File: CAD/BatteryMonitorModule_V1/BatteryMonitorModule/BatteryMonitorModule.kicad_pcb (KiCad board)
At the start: 2 copper layers, 76.2 x 101.6 mm, 85 parts, among them J1 OSTYK42105030, J10 J_DISP_SPI, J11 J_UART, J12 J_EXP_B, J13 J_EXP_A, J2 OSTYK42102030, J3 Conn_ARM_JTAG_SWD_10, J4 USB-C, J5 J_FAN, J6 J_FAN_SEL, J7 J_NFC, J8 J_PANEL, K1 G5LE-1, Q1 AO3401A, Q2 IRFZ44NPBF, Q3 MMBT2222A, Q4 MMBT2222A, Q5 2N7002, SW1 BOOT0, SW2 NRST, U1 STM32G0B1CCT6, U2 INA226AQDGSRQ1, U3 AP63205WU-7, U4 TC2117-3.3VDBTR

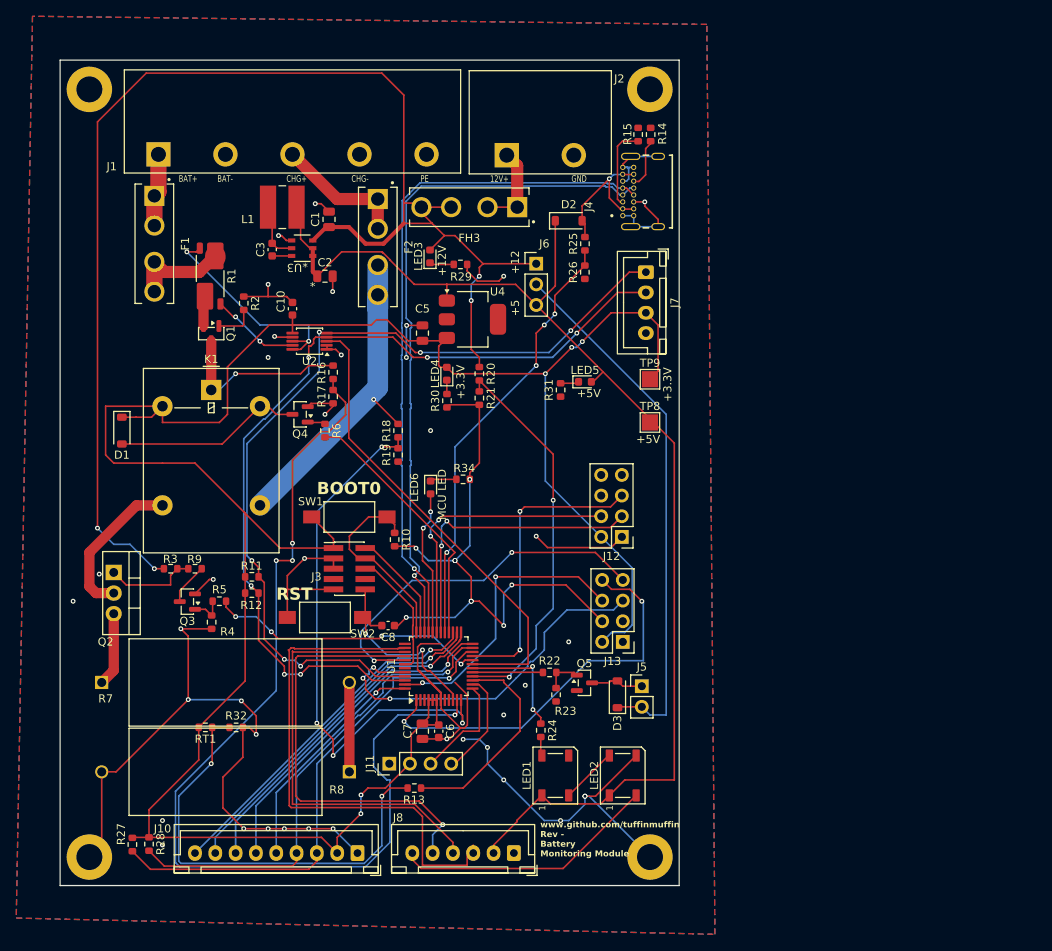
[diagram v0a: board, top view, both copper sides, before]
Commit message: V1 PCB layout updates and QT06ADP83H0000G footprint refinement
Co-Authored-By: Claude Opus 4.7 (1M context) <noreply@anthropic.com>
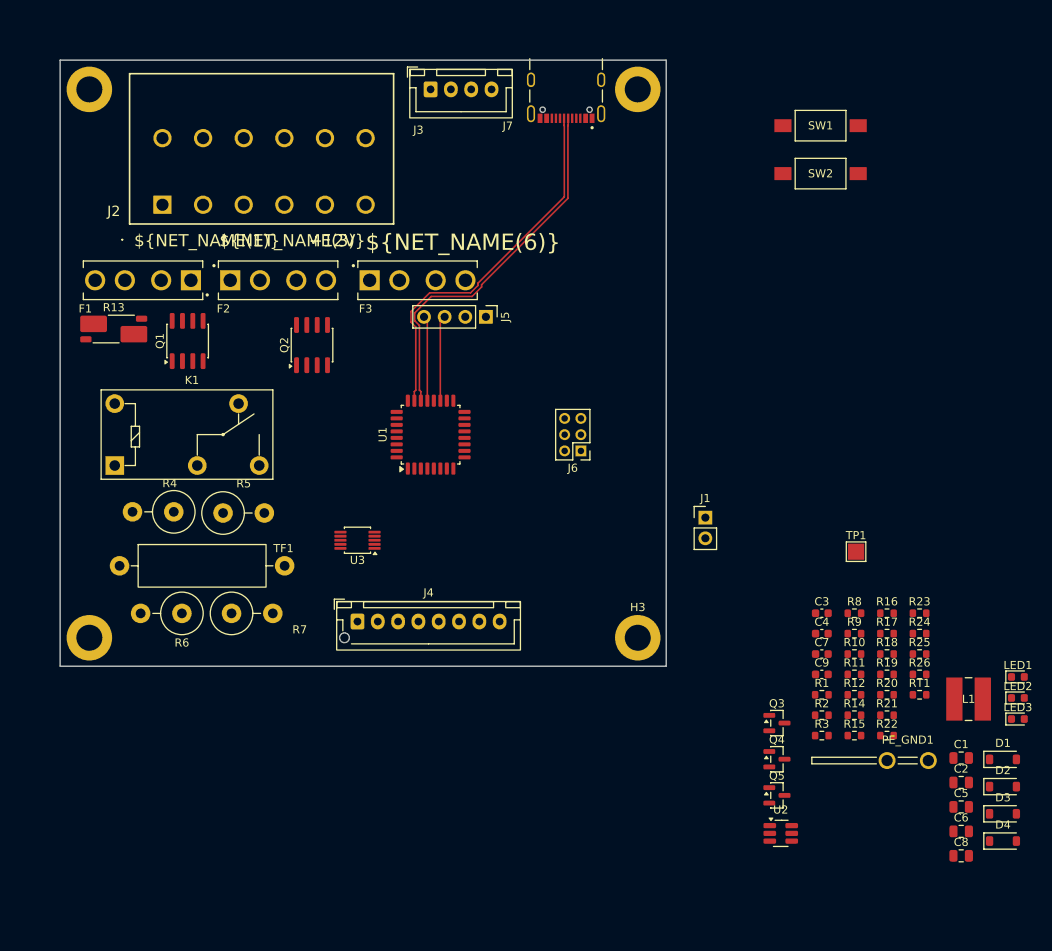
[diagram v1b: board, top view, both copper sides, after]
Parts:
- removed C10: 100nF, Capacitor_SMD:C_0603_1608Metric
- removed FH3: 2A ATM, BatteryMonitorModule_Custom:FUSE_BK-6013
- removed J10: J_DISP_SPI, Connector_JST:JST_XH_B9B-XH-A_1x09_P2.50mm_Vertical
- removed J11: J_UART, Connector_PinHeader_2.54mm:PinHeader_1x04_P2.54mm_Vertical
- removed J12: J_EXP_B, Connector_PinHeader_2.54mm:PinHeader_2x04_P2.54mm_Vertical
- removed J13: J_EXP_A, Connector_PinHeader_2.54mm:PinHeader_2x04_P2.54mm_Vertical
- removed J8: J_PANEL, Connector_JST:JST_XH_B6B-XH-A_1x06_P2.50mm_Vertical
- removed LED4: LED_3V3, LED_SMD:LED_0603_1608Metric
- removed LED5: LED_5V, LED_SMD:LED_0603_1608Metric
- removed LED6: LED_MCU, LED_SMD:LED_0603_1608Metric
- removed R27, R28: 4k7, Resistor_SMD:R_0603_1608Metric
- removed R29: 2k, Resistor_SMD:R_0603_1608Metric
- removed R30, R34: 270R, Resistor_SMD:R_0603_1608Metric
- removed R31: 560R, Resistor_SMD:R_0603_1608Metric
- removed R32: 10k, Resistor_SMD:R_0603_1608Metric
- removed TP8: 5V, TestPoint:TestPoint_Pad_2.0x2.0mm
- removed TP9: 3.3V, TestPoint:TestPoint_Pad_2.0x2.0mm
- removed U4: TC2117-3.3VDBTR, Package_TO_SOT_SMD:SOT-223-3_TabPin2
- added C4: 100nF, Capacitor_SMD:C_0603_1608Metric, F.Cu at (119.2, 96.0)
- added C9: 100nF, Capacitor_SMD:C_0603_1608Metric, F.Cu at (119.2, 101.0)
- added D4: 1N4148W, Diode_SMD:D_SOD-123, F.Cu at (141.5, 121.5)
- added F3: 2A ATM, BatteryMonitorModule_Custom:FUSE_BK-6013, F.Cu at (69.4, 52.5)
- added PE_GND1: Keystone 4966, BatteryMonitorModule_Custom:KEYSTONE_4966, F.Cu at (129.7, 111.6)
- added TF1: 184C, Resistor_THT:R_Axial_DIN0516_L15.5mm_D5.0mm_P20.32mm_Horizontal, F.Cu at (32.7, 87.6)
- added TP1: +3.3V, TestPoint:TestPoint_Pad_2.0x2.0mm, F.Cu at (123.4, 85.9)
- C1: value 10uF -> 100nF
- C2: value 22uF -> 10uF
- C5: value 10uF -> 22uF
- C6: value 100nF -> 22uF; footprint Capacitor_SMD:C_0603_1608Metric -> Capacitor_SMD:C_0805_2012Metric
- C7: value 4.7uF -> 100nF; footprint Capacitor_SMD:C_0805_2012Metric -> Capacitor_SMD:C_0603_1608Metric
- C8: value 100nF -> 4.7uF; footprint Capacitor_SMD:C_0603_1608Metric -> Capacitor_SMD:C_0805_2012Metric
- D2: value MBR0530 -> SS14
- D3: value 1N4148W -> SS14
- J1: value OSTYK42105030 -> J_FAN; footprint BatteryMonitorModule_Custom:OSTYK42105030 -> Connector_PinHeader_2.54mm:PinHeader_1x02_P2.54mm_Vertical
- J2: value OSTYK42102030 -> QT06ADP83H0000G; footprint BatteryMonitorModule_Custom:OSTYK42102030 -> BatteryMonitorModule_Custom:QT06ADP83H0000G
- J3: value Conn_ARM_JTAG_SWD_10 -> J_NFC; footprint Connector_PinHeader_1.27mm:PinHeader_2x05_P1.27mm_Vertical_SMD -> Connector_JST:JST_XH_B4B-XH-A_1x04_P2.50mm_Vertical
- J4: value USB-C -> J_PANEL; footprint BatteryMonitorModule_Custom:GCT_USB4085-GF-A_REVA4 -> Connector_JST:JST_XH_B8B-XH-AM_1x08_P2.50mm_Vertical
- J5: value J_FAN -> J_UART; footprint Connector_PinHeader_2.54mm:PinHeader_1x02_P2.54mm_Vertical -> Connector_PinHeader_2.54mm:PinHeader_1x04_P2.54mm_Vertical
- J6: value J_FAN_SEL -> Conn_ARM_JTAG_SWD_10; footprint Connector_PinHeader_2.54mm:PinHeader_1x03_P2.54mm_Vertical -> Connector_PinHeader_2.00mm:PinHeader_2x03_P2.00mm_Vertical
- J7: value J_NFC -> USB-C; footprint Connector_JST:JST_XH_B4B-XH-A_1x04_P2.50mm_Vertical -> BatteryMonitorModule_Custom:SAMESKY_UJ20-C-H-G-SMT-1-P16-TR
- K1: value G5LE-1 -> G5Q-14-DC12; footprint Relay_THT:Relay_SPDT_Omron-G5LE-1 -> Relay_THT:Relay_SPDT_Omron-G5Q-1
- L1: value 4.7uH -> 3.3uH
- LED1: value WS2812B -> LED_12V; footprint LED_SMD:LED_WS2812B_PLCC4_5.0x5.0mm_P3.2mm -> LED_SMD:LED_0603_1608Metric
- LED2: value WS2812B -> LED_3V3; footprint LED_SMD:LED_WS2812B_PLCC4_5.0x5.0mm_P3.2mm -> LED_SMD:LED_0603_1608Metric
- LED3: value LED_12V -> LED_MCU
- Q1: value AO3401A -> AO4407A; footprint Package_TO_SOT_SMD:SOT-23 -> Package_SO:SOIC-8_3.9x4.9mm_P1.27mm
- Q2: value IRFZ44NPBF -> AO4407A; footprint Package_TO_SOT_THT:TO-220-3_Vertical -> Package_SO:SOIC-8_3.9x4.9mm_P1.27mm
- Q3: value MMBT2222A -> AO3400A
- R1: value 10m -> 2k; footprint Resistor_SMD:R_Shunt_Vishay_WSK2512_6332Metric_T2.21mm -> Resistor_SMD:R_0603_1608Metric
- R10: value 10k -> 100k
- R11: value 4k7 -> 10k
- R12: value 4k7 -> 100R
- R13: value 100R -> 10m; footprint Resistor_SMD:R_0603_1608Metric -> Resistor_SMD:R_Shunt_Vishay_WSK2512_6332Metric_T2.21mm
- R14: value 5k1 -> 10k
- R15: value 5k1 -> 56k
- R16: value DNP -> 68k
- R17: value DNP -> 100
- R18: value DNP -> 1k
- R19: value DNP -> 10k
- R2, R3: value 10k -> 270R
- R20, R21: value DNP -> 4k7
- R22: value 100R -> 4k7
- R23: value 100k -> 4k7
- R24: value 470R -> 10k
- R25: value 82k -> 5k1
- R26: value 33k -> 5k1
- R4: value 100k -> 62.0 2W; footprint Resistor_SMD:R_0603_1608Metric -> Resistor_THT:R_Axial_DIN0516_L15.5mm_D5.0mm_P5.08mm_Vertical
- R5: value 4k7 -> 62.0 2W; footprint Resistor_SMD:R_0603_1608Metric -> Resistor_THT:R_Axial_DIN0516_L15.5mm_D5.0mm_P5.08mm_Vertical
- R6: value 1k -> 62.0 2W; footprint Resistor_SMD:R_0603_1608Metric -> Resistor_THT:R_Axial_DIN0516_L15.5mm_D5.0mm_P5.08mm_Vertical
- R7: value 3.3R 5W -> 62.0 2W; footprint BatteryMonitorModule_Custom:YAG_SQP500_YAG -> Resistor_THT:R_Axial_DIN0516_L15.5mm_D5.0mm_P5.08mm_Vertical
- R8: value 3.3R 5W -> 100R; footprint BatteryMonitorModule_Custom:YAG_SQP500_YAG -> Resistor_SMD:R_0603_1608Metric
- R9: value 100 -> 10k
- U1: value STM32G0B1CCT6 -> STM32C071K8T6; footprint Package_QFP:LQFP-48_7x7mm_P0.5mm -> Package_QFP:LQFP-32_7x7mm_P0.8mm
- U2: value INA226AQDGSRQ1 -> AP63203WU-7; footprint Package_SO:MSOP-10_3x3mm_P0.5mm -> Package_TO_SOT_SMD:SOT-23-6_Handsoldering
- U3: value AP63205WU-7 -> INA226AQDGSRQ1; footprint BatteryMonitorModule_Custom:AP63205WU-7_DIO -> Package_SO:MSOP-10_3x3mm_P0.5mm
- moved D1 115.8 mm to (141.5, 111.5), turned to 0 degrees
- moved L1 103.9 mm to (137.2, 104.0)
- moved C1 102.2 mm to (136.3, 111.3), turned to 0 degrees
- moved C2 100.1 mm to (136.3, 114.3)
- moved LED3 92.1 mm to (143.3, 106.5), turned to 0 degrees
- moved R1 91.2 mm to (119.2, 103.5), turned to 0 degrees
- moved C5 88.3 mm to (136.3, 117.3), turned to 0 degrees
- moved RT1 88.0 mm to (131.2, 103.5), turned to 0 degrees
- moved D2 87.8 mm to (141.5, 114.8)
- moved R2 87.4 mm to (119.2, 106.0), turned to 0 degrees
- moved U2 83.9 mm to (114.1, 120.6), turned to 0 degrees
- moved R3 82.7 mm to (119.2, 108.5)
- moved SW2 81.9 mm to (114.4, 39.4)
- moved R9 81.6 mm to (123.2, 96.0)
- moved C3 81.1 mm to (119.2, 93.5), turned to 0 degrees
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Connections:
- C1 pad 1: +12V -> VBUS_SENSE
- C2 pad 1: +5V -> VIn
- C3 pad 1: Net-(U3-BST) -> Net-(U2-BST)
- C3 pad 2: Net-(U3-SW) -> Net-(U2-SW)
- C8 pad 1: GND -> +3.3V
- C8 pad 2: /03-MCU/N_RST -> GND
- D1 pad 1: +3.3V -> +BATT
- D2 pad 1: +5V -> VIn
- D3 pad 1: Net-(D3-K) -> VIn
- F1 pad 1: Net-(J1-Pin_1) -> BATT+
- F2 pad 1: Net-(J1-Pin_3) -> CHARG+
- F2 pad 2: CHG_P_F2 -> Net-(F2-Pad2)
- H2 pad 1: unconnected-(H2-Pad1) -> GND
- J1 pad 1: Net-(J1-Pin_1) -> Net-(D1-A)
- J1 pad 2: GND -> +BATT
- J2 pad 1: Net-(J2-Pin_1) -> BATT+
- J3 pad 1: +3.3V -> I2C1_SCL
- J3 pad 2: SWDIO -> I2C1_SDA
- J3 pad 3: GND -> +3.3V
- J3 pad 4: BOOT0/SWDCLK -> GND
- J5 pad 1: Net-(D3-A) -> GND
- J5 pad 2: Net-(D3-K) -> +3.3V
- J6 pad 1: +12V -> +3.3V
- J6 pad 2: Net-(D3-K) -> SWDIO
- J6 pad 3: +5V -> GND
- K1 pad 1: BAT_P_FUSED -> BATT+
- K1 pad 2: +3.3V -> Net-(K1-Pad2)
- K1 pad 3: Net-(Q2-D) -> Net-(Q3-D)
- K1 pad 4: CHG_P_F2 -> BATT+
- K1 pad 5: Net-(D1-A) -> Net-(D4-A)
- L1 pad 1: Net-(U3-SW) -> Net-(U2-SW)
- L1 pad 2: +5V -> +3.3V
- LED1 pad 1: +5V -> Net-(LED1-K)
- LED1 pad 2: Net-(LED1-DOUT) -> VSup+
- LED2 pad 1: +5V -> Net-(LED2-K)
- LED2 pad 2: /04-IO/LED_DATA_O -> +3.3V
- LED3 pad 2: +12V -> MCU_LED
- Q1 pad 1: Net-(Q1-G) -> BATT+
- Q1 pad 2: Net-(Q1-S) -> BATT+
- Q1 pad 3: BAT_P_FUSED -> BATT+
- Q2 pad 1: Net-(Q2-G) -> Net-(K1-Pad2)
- Q2 pad 2: Net-(Q2-D) -> Net-(K1-Pad2)
- Q2 pad 3: Net-(Q2-S) -> Net-(K1-Pad2)
- Q3 pad 1: Net-(Q3-B) -> Net-(Q3-G)
- Q3 pad 2: GND -> /Load_Bank
- Q3 pad 3: Net-(Q3-C) -> Net-(Q3-D)
- Q4 pad 3: Net-(D1-A) -> Net-(D4-A)
- Q5 pad 1: Net-(Q5-G) -> FAN_PWM
- Q5 pad 3: Net-(D3-A) -> Net-(D1-A)
- R1 pad 1: Net-(F1-Pad2) -> GND
- R1 pad 2: SHUNT_P -> Net-(LED1-K)
- R10 pad 1: BOOT0/SWDCLK -> FAN_PWM
- R11 pad 1: +3.3V -> Net-(R11-Pad1)
- R11 pad 2: I2C1_SCL -> +3.3V
- R12 pad 1: +3.3V -> Net-(R11-Pad1)
- R12 pad 2: I2C1_SDA -> ADC_NTC
- R13 pad 1: Net-(R13-Pad1) -> Net-(F1-Pad2)
- R13 pad 2: ADC_NTC -> SHUNT_P
- R14 pad 1: Net-(J4-CC2) -> GND
- R14 pad 2: GND -> Net-(Q1-Pad4)
- R15 pad 1: Net-(J4-CC1) -> VBUS_SENSE
- R15 pad 2: GND -> +5VUsb
- R16 pad 1: BAT_P_FUSED -> GND
- R16 pad 2: ADC_BAT -> VBUS_SENSE
- R17 pad 1: ADC_BAT -> Net-(Q3-G)
- R17 pad 2: GND -> GPIO_BLEED
- R18 pad 1: CHG_P_F2 -> Net-(Q4-B)
- R18 pad 2: ADC_CHG -> GPIO_K1
- R19 pad 1: ADC_CHG -> GND
- R19 pad 2: GND -> Net-(Q3-G)
- R2 pad 2: Net-(Q1-G) -> Net-(LED2-K)
- R20 pad 1: +12V -> +3.3V
- R20 pad 2: ADC_12V -> I2C2_SDA
- R21 pad 1: ADC_12V -> +3.3V
- R21 pad 2: GND -> I2C2_SCL
- R22 pad 1: FAN_PWM -> +3.3V
- R22 pad 2: Net-(Q5-G) -> I2C1_SDA
- R23 pad 1: Net-(Q5-G) -> +3.3V
- R23 pad 2: GND -> I2C1_SCL
- R24 pad 1: LED_DATA -> BOOT0/SWDCLK
- R24 pad 2: Net-(LED1-DIN) -> Net-(R24-Pad2)
- R25 pad 1: VBUS_SENSE -> Net-(J7-CC1)
- R25 pad 2: +5VUsb -> GND
- R26 pad 1: GND -> Net-(J7-CC2)
- R26 pad 2: VBUS_SENSE -> GND
- R3 pad 1: +12V -> GND
- R3 pad 2: Net-(Q2-G) -> Net-(LED3-K)
- R4 pad 1: Net-(Q3-B) -> Net-(R4-Pad1)
- R5 pad 1: Net-(Q3-B) -> Net-(R4-Pad1)
- R5 pad 2: GPIO_BLEED -> GND
- R6 pad 1: Net-(Q4-B) -> Net-(R4-Pad1)
- R6 pad 2: GPIO_K1 -> GND
- R7 pad 1: Net-(Q2-S) -> Net-(R4-Pad1)
- R7 pad 2: Net-(R7-Pad2) -> GND
- R8 pad 1: Net-(R7-Pad2) -> FAN_PWM
- R8 pad 2: GND -> FAN_PWM
- R9 pad 1: Net-(Q2-G) -> GND
- R9 pad 2: Net-(Q3-C) -> Net-(Q2-Pad4)
- RT1 pad 1: Net-(R13-Pad1) -> Net-(R11-Pad1)
- RT1 pad 2: +3.3V -> GND
- SW1 pad 1: BOOT0/SWDCLK -> Net-(R24-Pad2)
- SW2 pad 2: /03-MCU/N_RST -> NRST
- U1 pad 1: J13-5 -> I2C1_SDA
- U1 pad 10: /03-MCU/N_RST -> GPIO_K1
- U1 pad 11: ADC_BAT -> GPIO_BLEED
- U1 pad 12: ADC_CHG -> SW_A
- U1 pad 13: UART2_TX -> unconnected-(U1-PA6-Pad13)
- U1 pad 14: UART2_RX -> unconnected-(U1-PA7-Pad14)
- U1 pad 15: ADC_NTC -> SW_B
- U1 pad 16: ADC_12V -> SW_C
- U1 pad 17: FAN_PWM -> SW_D
- U1 pad 18: LED_DATA -> unconnected-(U1-PA8-Pad18)
- U1 pad 19: INA_ALERT -> UART1_TX
- U1 pad 2: unconnected-(U1-PC14-Pad2) -> INA_ALERT
- U1 pad 20: GPIO_BLEED -> FAN_PWM
- U1 pad 21: J12-2 -> UART1_RX
- U1 pad 22: SPI2_SCK -> USB_D+
- U1 pad 23: SPI2_MOSI -> USB_D-
- U1 pad 24: SPI2_CS -> SWDIO
- U1 pad 25: SPI2_DC -> BOOT0/SWDCLK
- U1 pad 26: SPI2_RST -> unconnected-(U1-PA15-Pad26)
- U1 pad 27: BL_PWM -> unconnected-(U1-PB3-Pad27)
- U1 pad 28: GPIO_K1 -> unconnected-(U1-PB4-Pad28)
- U1 pad 29: VBUS_SENSE -> unconnected-(U1-PB5-Pad29)
- U1 pad 30: J12-0 -> MCU_LED
- U1 pad 31: J12-1 -> VBUS_SENSE
- U1 pad 32: MCU_HB -> I2C1_SCL
- U1 pad 5: +3.3V -> GND
- U1 pad 6: +3.3V -> NRST
- U1 pad 7: GND -> ADC_NTC
- U2 pad 1: GND -> +3.3V
- U2 pad 2: GND -> VIn
- U2 pad 3: INA_ALERT -> VIn
- U2 pad 4: I2C1_SDA -> GND
- U2 pad 5: I2C1_SCL -> Net-(U2-SW)
- U2 pad 6: +3.3V -> Net-(U2-BST)
- U3 pad 1: +5V -> GND
- U3 pad 2: +5V -> GND
- U3 pad 3: +12V -> INA_ALERT
- U3 pad 4: GND -> I2C1_SDA
- U3 pad 5: Net-(U3-SW) -> I2C1_SCL
- U3 pad 6: Net-(U3-BST) -> +3.3V
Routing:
- net GND: track 317.7 -> 0.00 mm, vias 48 -> 0
- net +3.3V: track 289.5 -> 0.00 mm, vias 5 -> 0
- net +12V: track 174.6 -> 0.00 mm, vias 4 -> 0
- net +5V: track 148.0 -> 0.00 mm
- net ADC_BAT: track 125.3 -> 0.00 mm, vias 4 -> 0
- net I2C1_SDA: track 108.5 -> 0.00 mm, vias 6 -> 0
- net I2C1_SCL: track 108.4 -> 0.00 mm, vias 6 -> 0
- net USB_DN: track 85.0 -> 0.00 mm, vias 1 -> 0
- net USB_DP: track 84.7 -> 0.00 mm, vias 1 -> 0
- net ADC_CHG: track 67.8 -> 0.00 mm, vias 4 -> 0
- net Net-(D3-K): track 66.1 -> 0.00 mm
- net SW_A: track 65.0 -> 0.00 mm
- net SPI2_SCK: track 62.3 -> 0.00 mm, vias 1 -> 0
- net SPI2_MOSI: track 59.3 -> 0.00 mm, vias 1 -> 0
- net INA_ALERT: track 57.8 -> 0.00 mm
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- removed copper zone on B.Cu, net GND
- removed copper zone on F.Cu, net GND
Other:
- board size 76.2 x 101.6 mm -> 74.6 x 74.6 mm
- board text removed: "+12V"
- board text removed: "+3.3V"
- board text removed: "+5V"
- board text removed: "BOOT0"
- board text removed: "MCU LED"
- board text removed: "RST"
- board text removed: "www.github.com/tuffinmuffin Rev - Battery Monitoring Module"
